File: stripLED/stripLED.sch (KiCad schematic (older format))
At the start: 24 parts, among them J1 Term, J2 Select, J3 Select, J4 Term, J8 Term, Q1 BSS138, Q10 2N7002, Q11 2N7002, Q12 2N7002, Q2 BSS138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

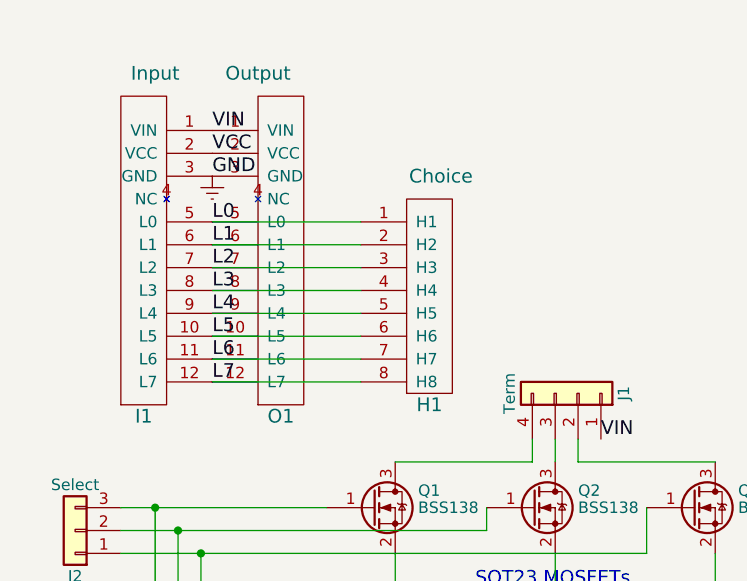
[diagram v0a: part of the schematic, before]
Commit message: More update to make the libraryies use only relative paths.
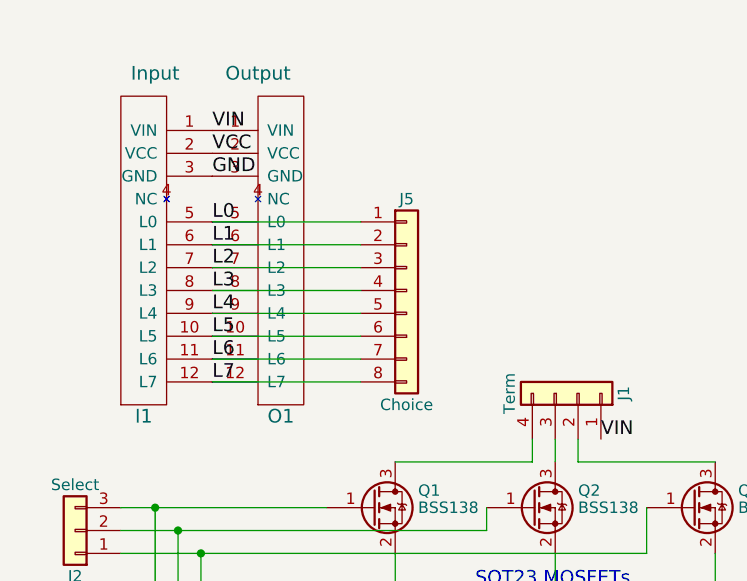
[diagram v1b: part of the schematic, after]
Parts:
- removed H1: Choice, Pin_Headers:Pin_Header_Straight_1x08_Pitch2.54mm, symbol Headers8L
- added J5: Choice, Pin_Headers:Pin_Header_Straight_1x08_Pitch2.54mm, symbol Conn_01x08
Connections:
- net L0: now also J5.1 (Pin_1)
- net L1: now also J5.2 (Pin_2)
- net L2: now also J5.3 (Pin_3)
- net L3: now also J5.4 (Pin_4)
- net L4: now also J5.5 (Pin_5)
- net L5: now also J5.6 (Pin_6)
- net L6: now also J5.7 (Pin_7)
- net L7: now also J5.8 (Pin_8)
- net Earth renamed GND
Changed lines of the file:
@@
 LIBS:valves
 LIBS:eplay
-LIBS:stripLED-cache
 EELAYER 25 0
 EELAYER END
@@
 L7
 $Comp
-L Earth #PWR01
-U 1 1 5AC24527
-P 2400 1950
-F 0 "#PWR01" H 2400 1700 50  0001 C CNN
-F 1 "Earth" H 2400 1800 50  0001 C CNN
-F 2 "" H 2400 1950 50  0001 C CNN
-F 3 "" H 2400 1950 50  0001 C CNN
-	1    2400 1950
-	1    0    0    -1
-$EndComp
-$Comp
 L Input I1
 U 1 1 5AC3D559
@@
 	0    1    -1   0
 $EndComp
-$Comp
-L Headers8L H1
-U 1 1 5AC82551
-P 3350 1900
-F 0 "H1" H 3350 850 60  0000 C CNN
-F 1 "Choice" H 3400 1850 60  0000 C CNN
-F 2 "Pin_Headers:Pin_Header_Straight_1x08_Pitch2.54mm" H 3400 1850 60  0001 C CNN
-F 3 "" H 3400 1850 60  0001 C CNN
-	1    3350 1900
-	1    0    0    -1
-$EndComp
 Text Label 4100 3100 0    60   ~ 0
 VIN
@@
 Text Label 8500 3750 0    60   ~ 0
 gate6
+$Comp
+L Conn_01x08 J5
+U 1 1 5AFF1C50
+P 3250 2450
+F 0 "J5" H 3250 2850 50  0000 C CNN
+F 1 "Choice" H 3250 1950 50  0000 C CNN
+F 2 "Pin_Headers:Pin_Header_Straight_1x08_Pitch2.54mm" H 3250 2450 50  0001 C CNN
+F 3 "" H 3250 2450 50  0001 C CNN
+	1    3250 2450
+	1    0    0    -1
+$EndComp
 $EndSCHEMATC
